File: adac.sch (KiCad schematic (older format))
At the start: 26 parts, among them J1 Conn_Coaxial, J2 Conn_Coaxial, J3 Conn_Coaxial, SW1 SW_SPST, U1 LTC1740, U2 TXS0108EPW, U3 TXS0108EPW, U4 AD7840

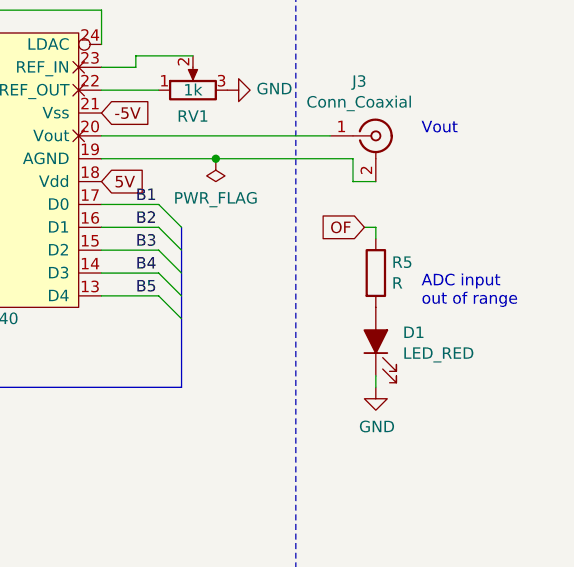
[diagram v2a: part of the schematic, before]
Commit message: Added footprints
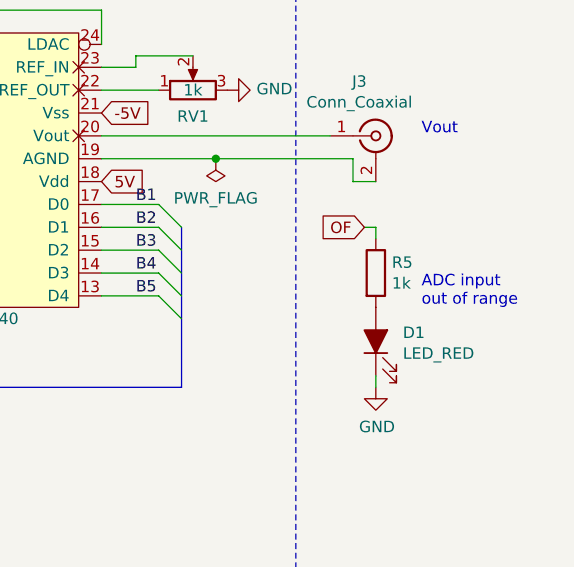
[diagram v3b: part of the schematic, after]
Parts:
- C1, C10, C2, C3, C4, C5, C6, C7, C8, C9: footprint (none) -> Capacitor_THT:C_Disc_D3.4mm_W2.1mm_P2.50mm
- D1: footprint (none) -> LED_THT:LED_D3.0mm
- J1, J2, J3: footprint (none) -> Connector_Coaxial:BNC_TEConnectivity_1478204_Vertical
- NT1: footprint (none) -> NetTie:NetTie-2_SMD_Pad0.5mm
- R1, R2, R3, R4: footprint (none) -> Resistor_THT:R_Axial_DIN0204_L3.6mm_D1.6mm_P7.62mm_Horizontal
- R5: value R -> 1k; footprint (none) -> Resistor_THT:R_Axial_DIN0204_L3.6mm_D1.6mm_P7.62mm_Horizontal
- RV1: footprint (none) -> Potentiometer_THT:Potentiometer_Bourns_3296W_Vertical
- SW1: footprint (none) -> Button_Switch_THT:SW_CuK_JS202011CQN_DPDT_Straight
- U1: footprint (none) -> Package_SO:SSOP-44_5.3x12.8mm_P0.5mm
- U4: footprint (none) -> Package_DIP:DIP-24_W7.62mm_LongPads
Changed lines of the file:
@@
 F 0 "C1" V 2350 3350 50  0000 C CNN
 F 1 "1u" V 2350 3550 50  0000 C CNN
-F 2 "" H 2438 3300 50  0001 C CNN
+F 2 "Capacitor_THT:C_Disc_D3.4mm_W2.1mm_P2.50mm" H 2438 3300 50  0001 C CNN
 F 3 "~" H 2400 3450 50  0001 C CNN
 	1    2400 3450
@@
 F 0 "C2" V 2350 3550 50  0000 C CNN
 F 1 "1u" V 2350 3750 50  0000 C CNN
-F 2 "" H 2438 3500 50  0001 C CNN
+F 2 "Capacitor_THT:C_Disc_D3.4mm_W2.1mm_P2.50mm" H 2438 3500 50  0001 C CNN
 F 3 "~" H 2400 3650 50  0001 C CNN
 	1    2400 3650
@@
 F 0 "C3" H 2715 3946 50  0000 L CNN
 F 1 "1u" H 2715 3855 50  0000 L CNN
-F 2 "" H 2638 3750 50  0001 C CNN
+F 2 "Capacitor_THT:C_Disc_D3.4mm_W2.1mm_P2.50mm" H 2638 3750 50  0001 C CNN
 F 3 "~" H 2600 3900 50  0001 C CNN
 	1    2600 3900
@@
 F 0 "C4" H 4865 3646 50  0000 L CNN
 F 1 "1u" H 4865 3555 50  0000 L CNN
-F 2 "" H 4788 3450 50  0001 C CNN
+F 2 "Capacitor_THT:C_Disc_D3.4mm_W2.1mm_P2.50mm" H 4788 3450 50  0001 C CNN
 F 3 "~" H 4750 3600 50  0001 C CNN
 	1    4750 3600
@@
 F 0 "C5" H 4865 3946 50  0000 L CNN
 F 1 "1u" H 4865 3855 50  0000 L CNN
-F 2 "" H 4788 3750 50  0001 C CNN
+F 2 "Capacitor_THT:C_Disc_D3.4mm_W2.1mm_P2.50mm" H 4788 3750 50  0001 C CNN
 F 3 "~" H 4750 3900 50  0001 C CNN
 	1    4750 3900
@@
 F 0 "U1" H 3500 5800 50  0000 C CNN
 F 1 "LTC1740" H 3500 4850 50  0000 C CNN
-F 2 "" H 4550 6150 50  0001 C CNN
+F 2 "Package_SO:SSOP-44_5.3x12.8mm_P0.5mm" H 4550 6150 50  0001 C CNN
 F 3 "" H 3600 5300 50  0001 C CNN
 	1    3500 4950
@@
 F 0 "C6" V 5900 2400 50  0000 C CNN
 F 1 "0u1" V 6100 2500 50  0000 C CNN
-F 2 "" H 5988 2350 50  0001 C CNN
+F 2 "Capacitor_THT:C_Disc_D3.4mm_W2.1mm_P2.50mm" H 5988 2350 50  0001 C CNN
 F 3 "~" H 5950 2500 50  0001 C CNN
 	1    5950 2500
@@
 F 0 "C8" V 6400 2400 50  0000 C CNN
 F 1 "0u1" V 6600 2500 50  0000 C CNN
-F 2 "" H 6488 2350 50  0001 C CNN
+F 2 "Capacitor_THT:C_Disc_D3.4mm_W2.1mm_P2.50mm" H 6488 2350 50  0001 C CNN
 F 3 "~" H 6450 2500 50  0001 C CNN
 	1    6450 2500
@@
 F 0 "C7" V 5900 4350 50  0000 C CNN
 F 1 "0u1" V 6100 4450 50  0000 C CNN
-F 2 "" H 5988 4300 50  0001 C CNN
+F 2 "Capacitor_THT:C_Disc_D3.4mm_W2.1mm_P2.50mm" H 5988 4300 50  0001 C CNN
 F 3 "~" H 5950 4450 50  0001 C CNN
 	1    5950 4450
@@
 F 0 "C9" V 6400 4350 50  0000 C CNN
 F 1 "0u1" V 6600 4450 50  0000 C CNN
-F 2 "" H 6488 4300 50  0001 C CNN
+F 2 "Capacitor_THT:C_Disc_D3.4mm_W2.1mm_P2.50mm" H 6488 4300 50  0001 C CNN
 F 3 "~" H 6450 4450 50  0001 C CNN
 	1    6450 4450
@@
 F 0 "R3" H 1670 3896 50  0000 L CNN
 F 1 "51R" H 1670 3805 50  0000 L CNN
-F 2 "" V 1530 3850 50  0001 C CNN
+F 2 "Resistor_THT:R_Axial_DIN0204_L3.6mm_D1.6mm_P7.62mm_Horizontal" V 1530 3850 50  0001 C CNN
 F 3 "~" H 1600 3850 50  0001 C CNN
 	1    1600 3850
@@
 F 0 "J2" H 1228 3938 50  0000 C CNN
 F 1 "Conn_Coaxial" H 1228 3847 50  0000 C CNN
-F 2 "" H 1300 3700 50  0001 C CNN
+F 2 "Connector_Coaxial:BNC_TEConnectivity_1478204_Vertical" H 1300 3700 50  0001 C CNN
 F 3 " ~" H 1300 3700 50  0001 C CNN
 	1    1300 3700
@@
 F 0 "R2" H 1670 3096 50  0000 L CNN
 F 1 "51R" H 1670 3005 50  0000 L CNN
-F 2 "" V 1530 3050 50  0001 C CNN
+F 2 "Resistor_THT:R_Axial_DIN0204_L3.6mm_D1.6mm_P7.62mm_Horizontal" V 1530 3050 50  0001 C CNN
 F 3 "~" H 1600 3050 50  0001 C CNN
 	1    1600 3050
@@
 F 0 "J1" H 1228 3138 50  0000 C CNN
 F 1 "Conn_Coaxial" H 1228 3047 50  0000 C CNN
-F 2 "" H 1300 2900 50  0001 C CNN
+F 2 "Connector_Coaxial:BNC_TEConnectivity_1478204_Vertical" H 1300 2900 50  0001 C CNN
 F 3 " ~" H 1300 2900 50  0001 C CNN
 	1    1300 2900
@@
 F 0 "J3" H 10328 4338 50  0000 C CNN
 F 1 "Conn_Coaxial" H 10328 4247 50  0000 C CNN
-F 2 "" H 10400 4100 50  0001 C CNN
+F 2 "Connector_Coaxial:BNC_TEConnectivity_1478204_Vertical" H 10400 4100 50  0001 C CNN
 F 3 " ~" H 10400 4100 50  0001 C CNN
 	1    10400 4100
@@
 F 0 "C10" V 8248 3300 50  0000 C CNN
 F 1 "0u1" V 8339 3300 50  0000 C CNN
-F 2 "" H 8538 3150 50  0001 C CNN
+F 2 "Capacitor_THT:C_Disc_D3.4mm_W2.1mm_P2.50mm" H 8538 3150 50  0001 C CNN
 F 3 "~" H 8500 3300 50  0001 C CNN
 	1    8500 3300
@@
 F 0 "R4" V 8693 3300 50  0000 C CNN
 F 1 "51R" V 8784 3300 50  0000 C CNN
-F 2 "" V 8830 3300 50  0001 C CNN
+F 2 "Resistor_THT:R_Axial_DIN0204_L3.6mm_D1.6mm_P7.62mm_Horizontal" V 8830 3300 50  0001 C CNN
 F 3 "~" H 8900 3300 50  0001 C CNN
 	1    8900 3300
@@
 F 0 "U4" H 8700 4250 50  0000 C CNN
 F 1 "AD7840" H 8700 3600 50  0000 C CNN
-F 2 "" H 9600 3050 50  0001 C CNN
+F 2 "Package_DIP:DIP-24_W7.62mm_LongPads" H 9600 3050 50  0001 C CNN
 F 3 "" H 9600 3050 50  0001 C CNN
 	1    8700 4250
@@
 F 0 "RV1" V 9485 3900 50  0000 C CNN
 F 1 "1k" V 9600 3900 50  0000 C CNN
-F 2 "" H 9600 3900 50  0001 C CNN
+F 2 "Potentiometer_THT:Potentiometer_Bourns_3296W_Vertical" H 9600 3900 50  0001 C CNN
 F 3 "~" H 9600 3900 50  0001 C CNN
 	1    9600 3900
@@
 F 0 "R1" H 1370 4596 50  0000 L CNN
 F 1 "10k" H 1370 4505 50  0000 L CNN
-F 2 "" V 1230 4550 50  0001 C CNN
+F 2 "Resistor_THT:R_Axial_DIN0204_L3.6mm_D1.6mm_P7.62mm_Horizontal" V 1230 4550 50  0001 C CNN
 F 3 "~" H 1300 4550 50  0001 C CNN
 	1    1300 4550
@@
 F 0 "SW1" V 1254 4912 50  0000 R CNN
 F 1 "SW_SPST" V 1345 4912 50  0000 R CNN
-F 2 "" H 1300 5000 50  0001 C CNN
+F 2 "Button_Switch_THT:SW_CuK_JS202011CQN_DPDT_Straight" H 1300 5000 50  0001 C CNN
 F 3 "~" H 1300 5000 50  0001 C CNN
 	1    1300 5000
@@
 P 10400 4700
 F 0 "R5" H 10470 4746 50  0000 L CNN
-F 1 "R" H 10470 4655 50  0000 L CNN
-F 2 "" V 10330 4700 50  0001 C CNN
+F 1 "1k" H 10470 4655 50  0000 L CNN
+F 2 "Resistor_THT:R_Axial_DIN0204_L3.6mm_D1.6mm_P7.62mm_Horizontal" V 10330 4700 50  0001 C CNN
 F 3 "~" H 10400 4700 50  0001 C CNN
 	1    10400 4700
@@
 F 0 "D1" V 10439 4882 50  0000 R CNN
 F 1 "LED_RED" V 10348 4882 50  0000 R CNN
-F 2 "" H 10400 5000 50  0001 C CNN
+F 2 "LED_THT:LED_D3.0mm" H 10400 5000 50  0001 C CNN
 F 3 "~" H 10400 5000 50  0001 C CNN
 	1    10400 5000
@@
 F 0 "NT1" H 5650 5831 50  0000 C CNN
 F 1 "Net-Tie_2" H 5650 5740 50  0000 C CNN
-F 2 "" H 5650 5650 50  0001 C CNN
+F 2 "NetTie:NetTie-2_SMD_Pad0.5mm" H 5650 5650 50  0001 C CNN
 F 3 "~" H 5650 5650 50  0001 C CNN
 	1    5650 5650
